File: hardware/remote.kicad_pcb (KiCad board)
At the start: 2 copper layers, 40 x 25 mm, 27 parts, among them J1 Debug, P1 CON-SENSOR2, P2 BOOT, U1 XMC1302-32, U2 RFM69HW, U3 DRILL, U4 DRILL, U5 DRILL, U6 DRILL

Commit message: specify led colors
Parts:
- D1: value LED -> blue
- D2: value LED -> green
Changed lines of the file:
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@@
       (effects (font (size 0.2 0.2) (thickness 0.05)))
     )
-    (fp_text value LED (at 0.75 0.45 90) (layer F.Fab)
+    (fp_text value blue (at 0.75 0.45 90) (layer F.Fab)
       (effects (font (size 0.2 0.2) (thickness 0.05)))
     )
@@
       (effects (font (size 0.2 0.2) (thickness 0.05)))
     )
-    (fp_text value LED (at 0.75 0.45 90) (layer F.Fab)
-      (effects (font (size 0.2 0.2) (thickness 0.05)))
-    )
+    (fp_text value green (at 0.75 0.45 90) (layer F.Fab)
+      (effects (font (size 0.2 0.2) (thickness 0.05)))
+    )

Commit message: fix broken mounting holes
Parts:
- U3, U4, U5, U6: footprint DRILL_NP -> kicad-libraries:DRILL_NP
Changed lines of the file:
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@@
     (34 B.Paste user)
     (35 F.Paste user)
-    (36 B.SilkS user)
-    (37 F.SilkS user)
+    (36 B.SilkS user hide)
+    (37 F.SilkS user hide)
     (38 B.Mask user)
     (39 F.Mask user)
@@
     (add_net Antenna)
   )
-  (module DRILL_NP (layer Vorderseite)
-    (at 80.4 32.3)
-    (solder_mask_margin 0.89916)
-    (clearance 0.89916)
-    (fp_text reference U3 (at 0 0) (layer F.SilkS) hide
-      (effects (font (size 0.29972 0.29972) (thickness 0.0762)))
-    )
-    (fp_text value DRILL (at 0 0.50038) (layer F.SilkS) hide
-      (effects (font (size 0.29972 0.29972) (thickness 0.0762)))
-    )
-    (fp_circle (center 0 0) (end 2.19964 -0.20066) (layer F.SilkS) (width 0.381))
-    (fp_circle (center 0 0) (end 1.99898 -0.20066) (layer F.SilkS) (width 0.381))
-    (fp_circle (center 0 0) (end 1.69926 0) (layer F.SilkS) (width 0.381))
-    (fp_circle (center 0 0) (end 1.39954 -0.09906) (layer B.SilkS) (width 0.381))
-    (fp_circle (center 0 0) (end 1.39954 0) (layer F.SilkS) (width 0.381))
-    (fp_circle (center 0 0) (end 1.69926 0) (layer B.SilkS) (width 0.381))
-    (fp_circle (center 0 0) (end 1.89992 0) (layer B.SilkS) (width 0.381))
-    (fp_circle (center 0 0) (end 2.19964 0) (layer B.SilkS) (width 0.381))
-    (pad "" thru_hole circle (at 0 0) (size 2.99974 2.99974) (drill 2.99974) (layers *.Cu *.SilkS *.Mask)
-      (clearance 0.89916))
-  )
-  (module DRILL_NP (layer Vorderseite)
-    (at 45.4 52.3)
-    (solder_mask_margin 0.89916)
-    (clearance 0.89916)
-    (fp_text reference U4 (at 0 0) (layer F.SilkS) hide
-      (effects (font (size 0.29972 0.29972) (thickness 0.0762)))
-    )
-    (fp_text value DRILL (at 0 0.50038) (layer F.SilkS) hide
-      (effects (font (size 0.29972 0.29972) (thickness 0.0762)))
-    )
-    (fp_circle (center 0 0) (end 2.19964 -0.20066) (layer F.SilkS) (width 0.381))
-    (fp_circle (center 0 0) (end 1.99898 -0.20066) (layer F.SilkS) (width 0.381))
-    (fp_circle (center 0 0) (end 1.69926 0) (layer F.SilkS) (width 0.381))
-    (fp_circle (center 0 0) (end 1.39954 -0.09906) (layer B.SilkS) (width 0.381))
-    (fp_circle (center 0 0) (end 1.39954 0) (layer F.SilkS) (width 0.381))
-    (fp_circle (center 0 0) (end 1.69926 0) (layer B.SilkS) (width 0.381))
-    (fp_circle (center 0 0) (end 1.89992 0) (layer B.SilkS) (width 0.381))
-    (fp_circle (center 0 0) (end 2.19964 0) (layer B.SilkS) (width 0.381))
-    (pad "" thru_hole circle (at 0 0) (size 2.99974 2.99974) (drill 2.99974) (layers *.Cu *.SilkS *.Mask)
-      (clearance 0.89916))
-  )
-  (module DRILL_NP (layer Vorderseite)
-    (at 45.4 32.3)
-    (solder_mask_margin 0.89916)
-    (clearance 0.89916)
-    (fp_text reference U6 (at 0 0) (layer F.SilkS) hide
-      (effects (font (size 0.29972 0.29972) (thickness 0.0762)))
-    )
-    (fp_text value DRILL (at 0 0.50038) (layer F.SilkS) hide
-      (effects (font (size 0.29972 0.29972) (thickness 0.0762)))
-    )
-    (fp_circle (center 0 0) (end 2.19964 -0.20066) (layer F.SilkS) (width 0.381))
-    (fp_circle (center 0 0) (end 1.99898 -0.20066) (layer F.SilkS) (width 0.381))
-    (fp_circle (center 0 0) (end 1.69926 0) (layer F.SilkS) (width 0.381))
-    (fp_circle (center 0 0) (end 1.39954 -0.09906) (layer B.SilkS) (width 0.381))
-    (fp_circle (center 0 0) (end 1.39954 0) (layer F.SilkS) (width 0.381))
-    (fp_circle (center 0 0) (end 1.69926 0) (layer B.SilkS) (width 0.381))
-    (fp_circle (center 0 0) (end 1.89992 0) (layer B.SilkS) (width 0.381))
-    (fp_circle (center 0 0) (end 2.19964 0) (layer B.SilkS) (width 0.381))
-    (pad "" thru_hole circle (at 0 0) (size 2.99974 2.99974) (drill 2.99974) (layers *.Cu *.SilkS *.Mask)
-      (clearance 0.89916))
-  )
-  (module DRILL_NP (layer Vorderseite)
-    (at 80.4 52.3)
-    (solder_mask_margin 0.89916)
-    (clearance 0.89916)
-    (fp_text reference U5 (at 0 0) (layer F.SilkS) hide
-      (effects (font (size 0.29972 0.29972) (thickness 0.0762)))
-    )
-    (fp_text value DRILL (at 0 0.50038) (layer F.SilkS) hide
-      (effects (font (size 0.29972 0.29972) (thickness 0.0762)))
-    )
-    (fp_circle (center 0 0) (end 2.19964 -0.20066) (layer F.SilkS) (width 0.381))
-    (fp_circle (center 0 0) (end 1.99898 -0.20066) (layer F.SilkS) (width 0.381))
-    (fp_circle (center 0 0) (end 1.69926 0) (layer F.SilkS) (width 0.381))
-    (fp_circle (center 0 0) (end 1.39954 -0.09906) (layer B.SilkS) (width 0.381))
-    (fp_circle (center 0 0) (end 1.39954 0) (layer F.SilkS) (width 0.381))
-    (fp_circle (center 0 0) (end 1.69926 0) (layer B.SilkS) (width 0.381))
-    (fp_circle (center 0 0) (end 1.89992 0) (layer B.SilkS) (width 0.381))
-    (fp_circle (center 0 0) (end 2.19964 0) (layer B.SilkS) (width 0.381))
-    (pad "" thru_hole circle (at 0 0) (size 2.99974 2.99974) (drill 2.99974) (layers *.Cu *.SilkS *.Mask)
-      (clearance 0.89916))
-  )
   (module Fiducial_Mark (layer Vorderseite)
     (at 63.4 47.3)
@@
       (net 28 "Net-(J1-Pad1)"))
   )
+  (module kicad-libraries:DRILL_NP (layer Vorderseite)
+    (at 80.4 52.3)
+    (fp_text reference U5 (at 0 0) (layer F.SilkS) hide
+      (effects (font (size 0.29972 0.29972) (thickness 0.0762)))
+    )
+    (fp_text value DRILL (at 0 0.50038) (layer F.SilkS) hide
+      (effects (font (size 0.29972 0.29972) (thickness 0.0762)))
+    )
+    (fp_circle (center 0 0) (end 3.2 0) (layer Eco2.User) (width 0.01))
+    (fp_circle (center 0 0) (end 2.19964 -0.20066) (layer F.SilkS) (width 0.381))
+    (fp_circle (center 0 0) (end 1.99898 -0.20066) (layer F.SilkS) (width 0.381))
+    (fp_circle (center 0 0) (end 1.69926 0) (layer F.SilkS) (width 0.381))
+    (fp_circle (center 0 0) (end 1.39954 -0.09906) (layer B.SilkS) (width 0.381))
+    (fp_circle (center 0 0) (end 1.39954 0) (layer F.SilkS) (width 0.381))
+    (fp_circle (center 0 0) (end 1.69926 0) (layer B.SilkS) (width 0.381))
+    (fp_circle (center 0 0) (end 1.89992 0) (layer B.SilkS) (width 0.381))
+    (fp_circle (center 0 0) (end 2.19964 0) (layer B.SilkS) (width 0.381))
+    (pad "" np_thru_hole circle (at 0 0) (size 2.99974 2.99974) (drill 2.99974) (layers *.Cu *.Mask F.SilkS)
+      (clearance 0.89916))
+  )
+  (module kicad-libraries:DRILL_NP (layer Vorderseite)
+    (at 45.4 32.3)
+    (fp_text reference U6 (at 0 0) (layer F.SilkS) hide
+      (effects (font (size 0.29972 0.29972) (thickness 0.0762)))
+    )
+    (fp_text value DRILL (at 0 0.50038) (layer F.SilkS) hide
+      (effects (font (size 0.29972 0.29972) (thickness 0.0762)))
+    )
+    (fp_circle (center 0 0) (end 3.2 0) (layer Eco2.User) (width 0.01))
+    (fp_circle (center 0 0) (end 2.19964 -0.20066) (layer F.SilkS) (width 0.381))
+    (fp_circle (center 0 0) (end 1.99898 -0.20066) (layer F.SilkS) (width 0.381))
+    (fp_circle (center 0 0) (end 1.69926 0) (layer F.SilkS) (width 0.381))
+    (fp_circle (center 0 0) (end 1.39954 -0.09906) (layer B.SilkS) (width 0.381))
+    (fp_circle (center 0 0) (end 1.39954 0) (layer F.SilkS) (width 0.381))
+    (fp_circle (center 0 0) (end 1.69926 0) (layer B.SilkS) (width 0.381))
+    (fp_circle (center 0 0) (end 1.89992 0) (layer B.SilkS) (width 0.381))
+    (fp_circle (center 0 0) (end 2.19964 0) (layer B.SilkS) (width 0.381))
+    (pad "" np_thru_hole circle (at 0 0) (size 2.99974 2.99974) (drill 2.99974) (layers *.Cu *.Mask F.SilkS)
+      (clearance 0.89916))
+  )
+  (module kicad-libraries:DRILL_NP (layer Vorderseite)
+    (at 45.4 52.3)
+    (fp_text reference U4 (at 0 0) (layer F.SilkS) hide
+      (effects (font (size 0.29972 0.29972) (thickness 0.0762)))
+    )
+    (fp_text value DRILL (at 0 0.50038) (layer F.SilkS) hide
+      (effects (font (size 0.29972 0.29972) (thickness 0.0762)))
+    )
+    (fp_circle (center 0 0) (end 3.2 0) (layer Eco2.User) (width 0.01))
+    (fp_circle (center 0 0) (end 2.19964 -0.20066) (layer F.SilkS) (width 0.381))
+    (fp_circle (center 0 0) (end 1.99898 -0.20066) (layer F.SilkS) (width 0.381))
+    (fp_circle (center 0 0) (end 1.69926 0) (layer F.SilkS) (width 0.381))
+    (fp_circle (center 0 0) (end 1.39954 -0.09906) (layer B.SilkS) (width 0.381))
+    (fp_circle (center 0 0) (end 1.39954 0) (layer F.SilkS) (width 0.381))
+    (fp_circle (center 0 0) (end 1.69926 0) (layer B.SilkS) (width 0.381))
+    (fp_circle (center 0 0) (end 1.89992 0) (layer B.SilkS) (width 0.381))
+    (fp_circle (center 0 0) (end 2.19964 0) (layer B.SilkS) (width 0.381))
+    (pad "" np_thru_hole circle (at 0 0) (size 2.99974 2.99974) (drill 2.99974) (layers *.Cu *.Mask F.SilkS)
+      (clearance 0.89916))
+  )
+  (module kicad-libraries:DRILL_NP (layer Vorderseite)
+    (at 80.4 32.3)
+    (fp_text reference U3 (at 0 0) (layer F.SilkS) hide
+      (effects (font (size 0.29972 0.29972) (thickness 0.0762)))
+    )
+    (fp_text value DRILL (at 0 0.50038) (layer F.SilkS) hide
+      (effects (font (size 0.29972 0.29972) (thickness 0.0762)))
+    )
+    (fp_circle (center 0 0) (end 3.2 0) (layer Eco2.User) (width 0.01))
+    (fp_circle (center 0 0) (end 2.19964 -0.20066) (layer F.SilkS) (width 0.381))
+    (fp_circle (center 0 0) (end 1.99898 -0.20066) (layer F.SilkS) (width 0.381))
+    (fp_circle (center 0 0) (end 1.69926 0) (layer F.SilkS) (width 0.381))
+    (fp_circle (center 0 0) (end 1.39954 -0.09906) (layer B.SilkS) (width 0.381))
+    (fp_circle (center 0 0) (end 1.39954 0) (layer F.SilkS) (width 0.381))
+    (fp_circle (center 0 0) (end 1.69926 0) (layer B.SilkS) (width 0.381))
+    (fp_circle (center 0 0) (end 1.89992 0) (layer B.SilkS) (width 0.381))
+    (fp_circle (center 0 0) (end 2.19964 0) (layer B.SilkS) (width 0.381))
+    (pad "" np_thru_hole circle (at 0 0) (size 2.99974 2.99974) (drill 2.99974) (layers *.Cu *.Mask F.SilkS)
+      (clearance 0.89916))
+  )
   (gr_line (start 82.9 32.3) (end 82.9 39.1) (angle 90) (layer Edge.Cuts) (width 0.381))

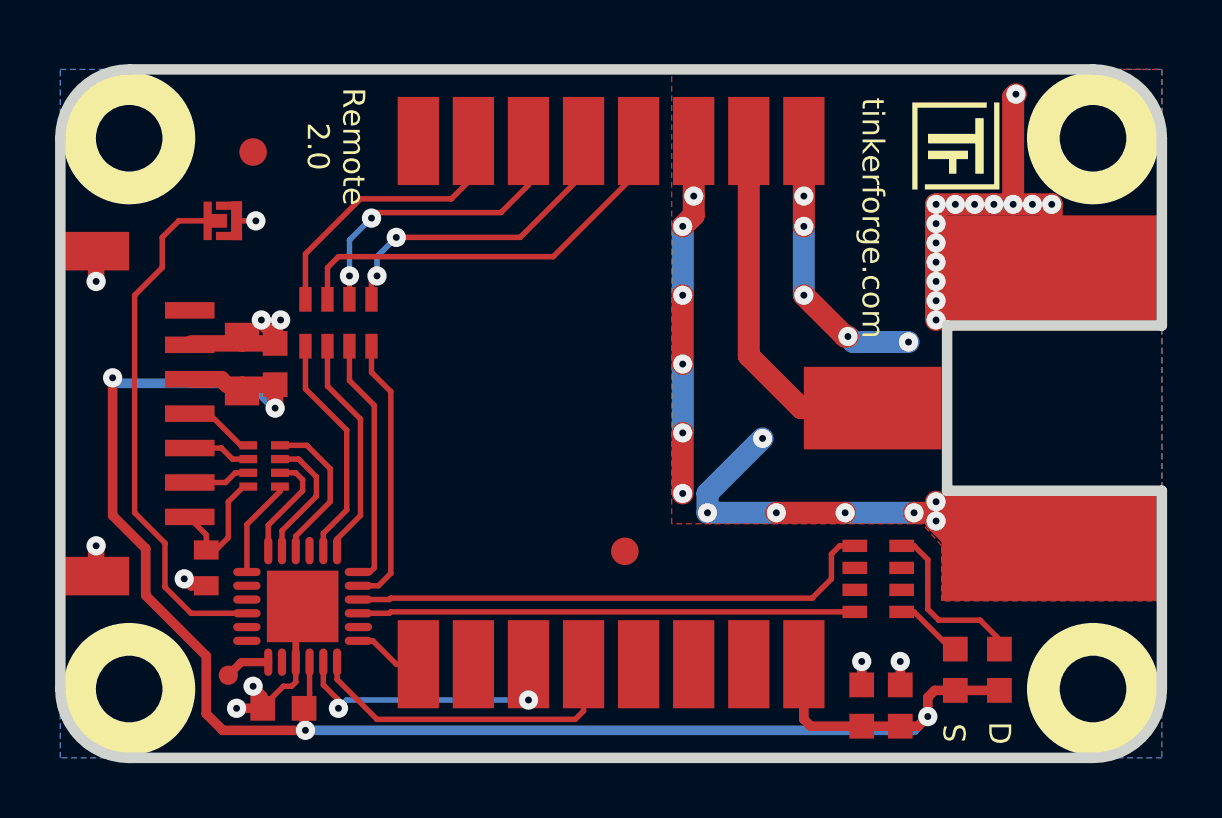
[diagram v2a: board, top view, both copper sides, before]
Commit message: Fix egde cuts
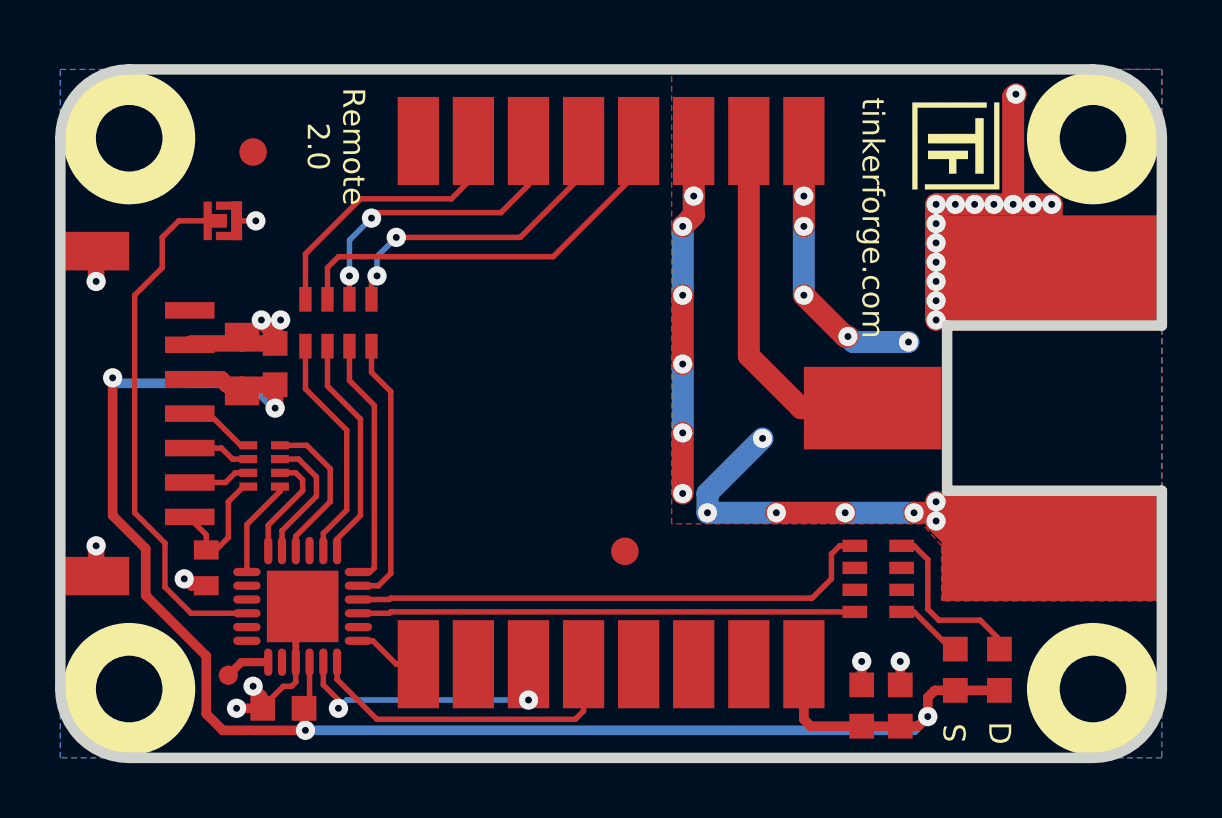
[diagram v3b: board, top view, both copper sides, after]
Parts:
- ANT1: footprint FT-004B -> kicad-libraries:FT-004B
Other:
- outline, holes or cut-outs redrawn
